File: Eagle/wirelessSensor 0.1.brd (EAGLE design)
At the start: 25.1 x 25.4 mm, 22 parts, among them U1 HDC1080, U2 PIC16F1823-X_SL, X1 22-23-2021

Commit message: Started working on the ESP8266, having some trouble with buffer overrun on the PIC.  Started some board layout
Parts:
- added R4: 10k, rcl:R0603
- moved U$1 45.5 mm to (5.08, 34.3)
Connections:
- new net N$7: R4.1, U$1.3
- net N$1: now also U$1.22; no longer U$1.21
- net N$8: now also U$1.21; no longer U$1.22
- net VCC: now also R4.2
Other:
- board size 25.1 x 25.4 mm -> 25.1 x 50.8 mm
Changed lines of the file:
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@@
 <?xml version="1.0" encoding="utf-8"?>
 <!DOCTYPE eagle SYSTEM "eagle.dtd">
-<eagle version="7.7.0">
+<eagle version="7.6.0">
 <drawing>
 <settings>
@@
 <plain>
 <wire x1="0" y1="0" x2="25.07" y2="0" width="0" layer="20"/>
-<wire x1="25.07" y1="0" x2="25.07" y2="25.39" width="0" layer="20"/>
-<wire x1="25.07" y1="25.39" x2="0" y2="25.39" width="0" layer="20"/>
-<wire x1="0" y1="25.39" x2="0" y2="0" width="0" layer="20"/>
+<wire x1="25.07" y1="0" x2="25.07" y2="50.79" width="0" layer="20"/>
+<wire x1="25.07" y1="50.79" x2="0" y2="50.79" width="0" layer="20"/>
+<wire x1="0" y1="50.79" x2="0" y2="0" width="0" layer="20"/>
 </plain>
 <attributes>
@@
 <element name="LED1" library="led" package="CHIP-LED0603" value="" x="22.86" y="10.16"/>
 <element name="R3" library="rcl" package="R0603" value="330" x="20.32" y="10.16" rot="R90"/>
-<element name="U$1" library="wirelessSensor" package="ESP8266-12E" value="ESP8266-12E" x="-21.59" y="-2.54"/>
+<element name="U$1" library="wirelessSensor" package="ESP8266-12E" value="ESP8266-12E" x="5.08" y="34.29"/>
+<element name="R4" library="rcl" package="R0603" value="10k" x="1.27" y="40.64" rot="R270"/>
 </elements>
 <signals>
@@
 <contactref element="C4" pad="1"/>
 <contactref element="C3" pad="1"/>
+<contactref element="R4" pad="2"/>
 <wire x1="19.47" y1="16.51" x2="22.86" y2="21.59" width="0" layer="19" extent="1-1"/>
 <wire x1="10.3378" y1="15.24" x2="19.47" y2="16.51" width="0" layer="19" extent="1-1"/>
@@
 <wire x1="4.205" y1="1.27" x2="4.205" y2="3.81" width="0" layer="19" extent="1-1"/>
 <wire x1="3.81" y1="24.13" x2="5.209996875" y2="17.78" width="0" layer="19" extent="1-1"/>
-<wire x1="-21.59" y1="-1.04" x2="4.205" y2="1.27" width="0" layer="19" extent="1-1"/>
+<wire x1="1.27" y1="39.79" x2="4.205" y2="1.27" width="0" layer="19" extent="1-1"/>
+<wire x1="5.08" y1="35.79" x2="1.27" y2="39.79" width="0" layer="19" extent="1-1"/>
 </signal>
 <signal name="GND">
@@
 <wire x1="5.955" y1="3.81" x2="5.955" y2="6.35" width="0" layer="19" extent="1-1"/>
 <wire x1="5.955" y1="1.27" x2="5.955" y2="3.81" width="0" layer="19" extent="1-1"/>
-<wire x1="-5.59" y1="-1.04" x2="5.955" y2="1.27" width="0" layer="19" extent="1-1"/>
+<wire x1="21.08" y1="35.79" x2="5.955" y2="1.27" width="0" layer="19" extent="1-1"/>
 </signal>
 <signal name="N$2">
@@
 </signal>
 <signal name="N$8">
-<contactref element="U$1" pad="22"/>
 <contactref element="U2" pad="6"/>
 <contactref element="TX" pad="TP"/>
+<contactref element="U$1" pad="21"/>
 <wire x1="1.27" y1="3.81" x2="10.3378" y2="8.89" width="0" layer="19" extent="1-1"/>
-<wire x1="-5.59" y1="12.96" x2="1.27" y2="3.81" width="0" layer="19" extent="1-1"/>
+<wire x1="21.08" y1="47.79" x2="1.27" y2="3.81" width="0" layer="19" extent="1-1"/>
 </signal>
 <signal name="N$1">
 <contactref element="U2" pad="5"/>
 <contactref element="RX" pad="TP"/>
-<contactref element="U$1" pad="21"/>
+<contactref element="U$1" pad="22"/>
 <wire x1="1.27" y1="1.27" x2="10.3378" y2="10.16" width="0" layer="19" extent="1-1"/>
-<wire x1="-5.59" y1="10.96" x2="1.27" y2="1.27" width="0" layer="19" extent="1-1"/>
+<wire x1="21.08" y1="49.79" x2="1.27" y2="1.27" width="0" layer="19" extent="1-1"/>
+</signal>
+<signal name="N$7">
+<contactref element="R4" pad="1"/>
+<contactref element="U$1" pad="3"/>
+<wire x1="5.08" y1="45.79" x2="1.27" y2="41.49" width="0" layer="19" extent="1-1"/>
 </signal>
 </signals>

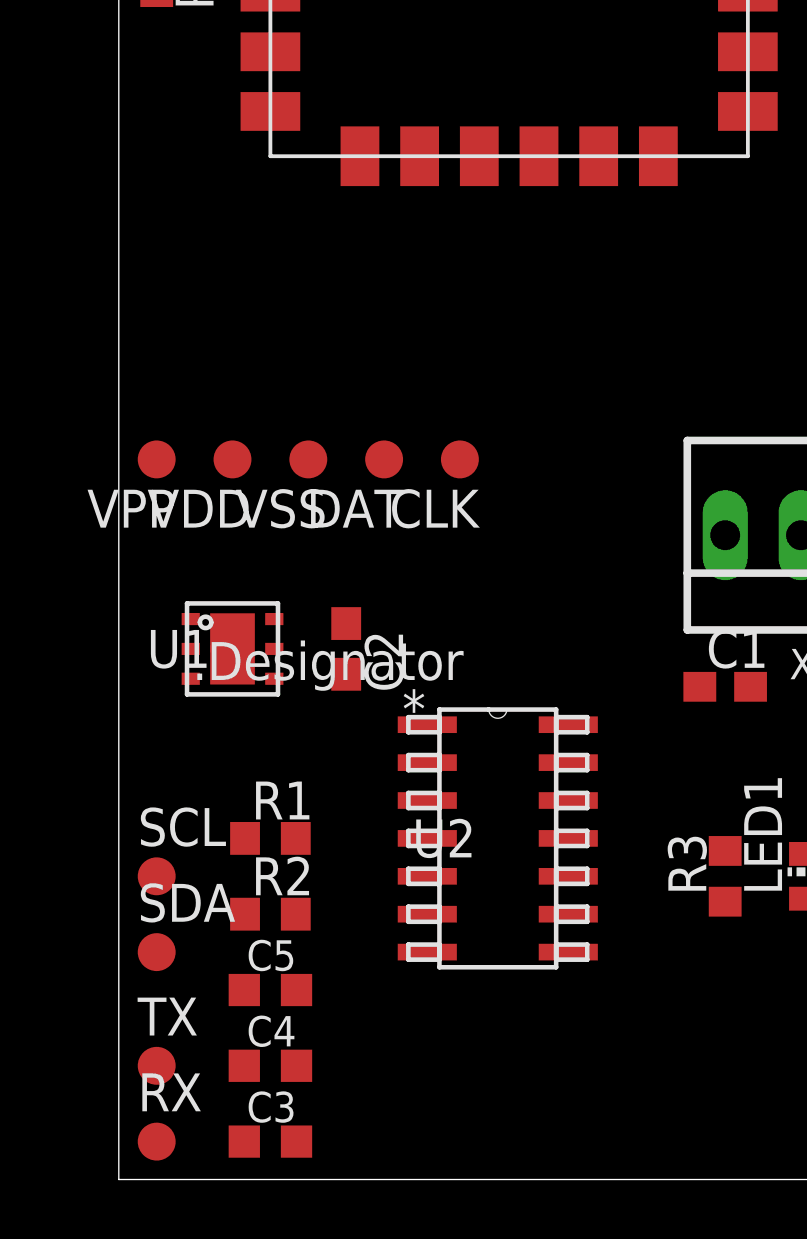
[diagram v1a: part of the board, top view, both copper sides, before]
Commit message: Wrapping up the schematic before board order; minor firmware adjustments; added CAM file for Gerber generation
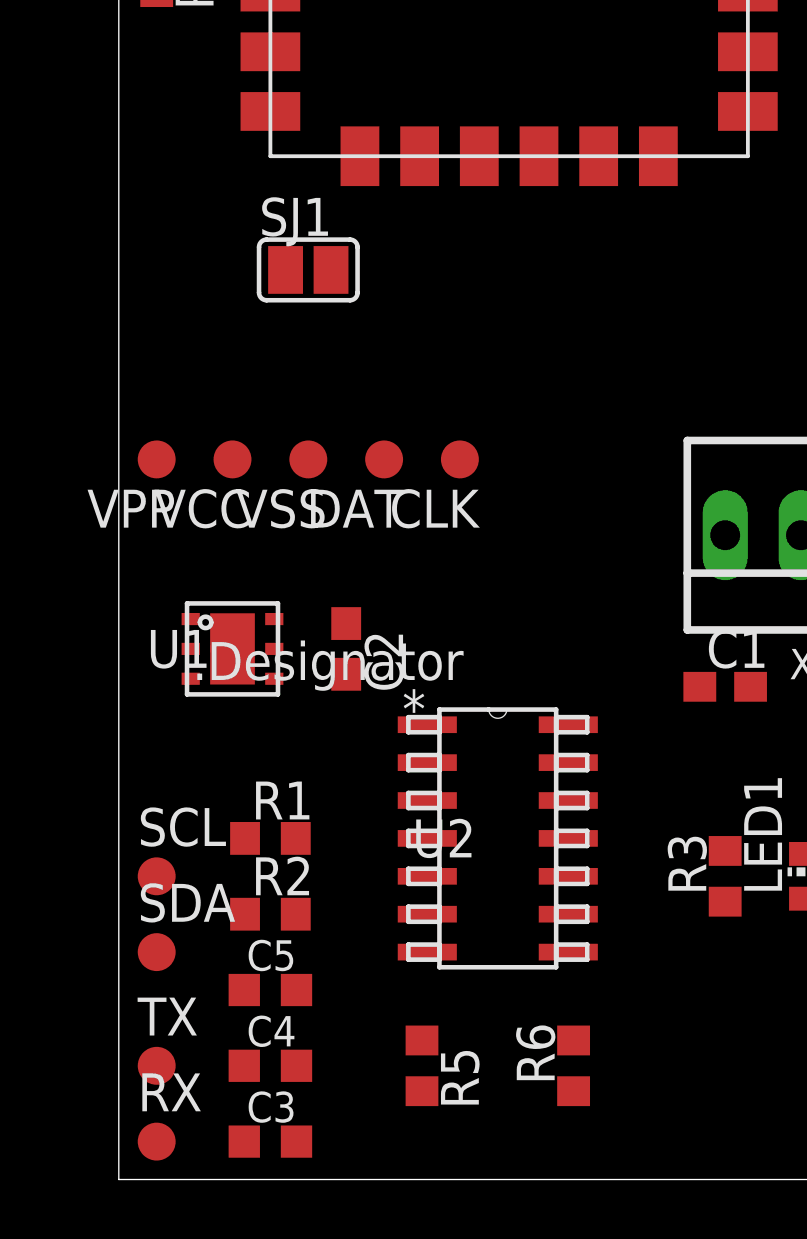
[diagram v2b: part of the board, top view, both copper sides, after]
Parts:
- added R5, R6: SEL, rcl:R0603
- added SJ1: (no value), jumper:SJ
- renumbered VDD to VCC
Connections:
- new net N$12: SJ1.1, U$1.2
- new net N$9: R5.1, R6.2, SJ1.2, U2.3
- net GND: now also R6.1
- net VCC: now also R5.2
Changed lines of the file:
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@@
 <?xml version="1.0" encoding="utf-8"?>
 <!DOCTYPE eagle SYSTEM "eagle.dtd">
-<eagle version="7.6.0">
+<eagle version="7.7.0">
 <drawing>
 <settings>
@@
 </element>
 <element name="U2" library="wirelessSensor" package="SOIC14-N_MC" value="PIC16F1823-X_SL" x="12.7" y="11.43"/>
-<element name="VDD" library="testpad" package="B1,27" value="TPB1,27" x="3.81" y="24.13" rot="R180">
+<element name="VCC" library="testpad" package="B1,27" value="TPB1,27" x="3.81" y="24.13" rot="R180">
 <attribute name="TP_SIGNAL_NAME" value="" x="3.81" y="24.13" size="1.778" layer="27" rot="R180" display="off"/>
 </element>
@@
 <element name="U$1" library="wirelessSensor" package="ESP8266-12E" value="ESP8266-12E" x="5.08" y="34.29"/>
 <element name="R4" library="rcl" package="R0603" value="10k" x="1.27" y="40.64" rot="R270"/>
+<element name="R5" library="rcl" package="R0603" value="SEL" x="10.16" y="3.81" rot="R270"/>
+<element name="R6" library="rcl" package="R0603" value="SEL" x="15.24" y="3.81" rot="R90"/>
+<element name="SJ1" library="jumper" package="SJ" value="" x="6.35" y="30.48"/>
 </elements>
 <signals>
@@
 <contactref element="U2" pad="1"/>
 <contactref element="U1" pad="5"/>
-<contactref element="VDD" pad="TP"/>
+<contactref element="VCC" pad="TP"/>
 <contactref element="C2" pad="1"/>
 <contactref element="C5" pad="1"/>
@@
 <contactref element="C3" pad="1"/>
 <contactref element="R4" pad="2"/>
+<contactref element="R5" pad="2"/>
 <wire x1="19.47" y1="16.51" x2="22.86" y2="21.59" width="0" layer="19" extent="1-1"/>
 <wire x1="10.3378" y1="15.24" x2="19.47" y2="16.51" width="0" layer="19" extent="1-1"/>
@@
 <wire x1="4.205" y1="3.81" x2="4.205" y2="6.35" width="0" layer="19" extent="1-1"/>
 <wire x1="4.205" y1="1.27" x2="4.205" y2="3.81" width="0" layer="19" extent="1-1"/>
+<wire x1="10.16" y1="2.96" x2="4.205" y2="1.27" width="0" layer="19" extent="1-1"/>
 <wire x1="3.81" y1="24.13" x2="5.209996875" y2="17.78" width="0" layer="19" extent="1-1"/>
-<wire x1="1.27" y1="39.79" x2="4.205" y2="1.27" width="0" layer="19" extent="1-1"/>
-<wire x1="5.08" y1="35.79" x2="1.27" y2="39.79" width="0" layer="19" extent="1-1"/>
+<wire x1="5.08" y1="35.79" x2="3.81" y2="24.13" width="0" layer="19" extent="1-1"/>
+<wire x1="1.27" y1="39.79" x2="5.08" y2="35.79" width="0" layer="19" extent="1-1"/>
 </signal>
 <signal name="GND">
@@
 <contactref element="C4" pad="2"/>
 <contactref element="C3" pad="2"/>
+<contactref element="R6" pad="1"/>
+<wire x1="20.32" y1="21.59" x2="21.08" y2="35.79" width="0" layer="19" extent="1-1"/>
 <wire x1="21.17" y1="16.51" x2="20.32" y2="21.59" width="0" layer="19" extent="1-1"/>
 <wire x1="15.0622" y1="15.24" x2="21.17" y2="16.51" width="0" layer="19" extent="1-1"/>
@@
 <wire x1="5.955" y1="3.81" x2="5.955" y2="6.35" width="0" layer="19" extent="1-1"/>
 <wire x1="5.955" y1="1.27" x2="5.955" y2="3.81" width="0" layer="19" extent="1-1"/>
-<wire x1="21.08" y1="35.79" x2="5.955" y2="1.27" width="0" layer="19" extent="1-1"/>
+<wire x1="15.24" y1="2.96" x2="5.955" y2="1.27" width="0" layer="19" extent="1-1"/>
 </signal>
 <signal name="N$2">
@@
 <wire x1="5.08" y1="45.79" x2="1.27" y2="41.49" width="0" layer="19" extent="1-1"/>
 </signal>
+<signal name="N$9">
+<contactref element="R6" pad="2"/>
+<contactref element="R5" pad="1"/>
+<contactref element="U2" pad="3"/>
+<contactref element="SJ1" pad="2"/>
+<wire x1="10.16" y1="4.66" x2="10.3378" y2="12.7" width="0" layer="19" extent="1-1"/>
+<wire x1="15.24" y1="4.66" x2="10.16" y2="4.66" width="0" layer="19" extent="1-1"/>
+<wire x1="7.112" y1="30.48" x2="10.16" y2="4.66" width="0" layer="19" extent="1-1"/>
+</signal>
+<signal name="N$12">
+<contactref element="SJ1" pad="1"/>
+<contactref element="U$1" pad="2"/>
+<wire x1="5.588" y1="30.48" x2="5.08" y2="47.79" width="0" layer="19" extent="1-1"/>
+</signal>
 </signals>

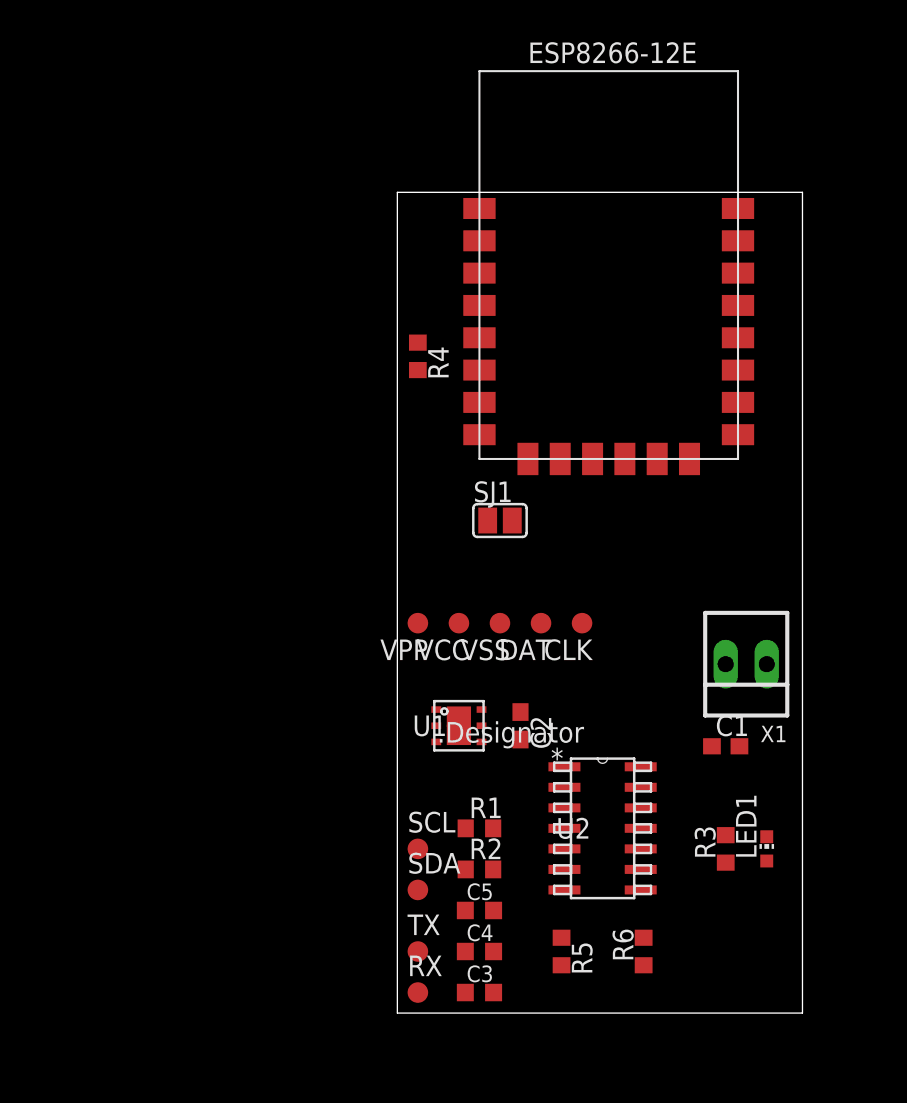
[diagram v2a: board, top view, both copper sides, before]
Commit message: More work on the PCB, added some SeeedStudio specific files (cam generator, DRC rules)
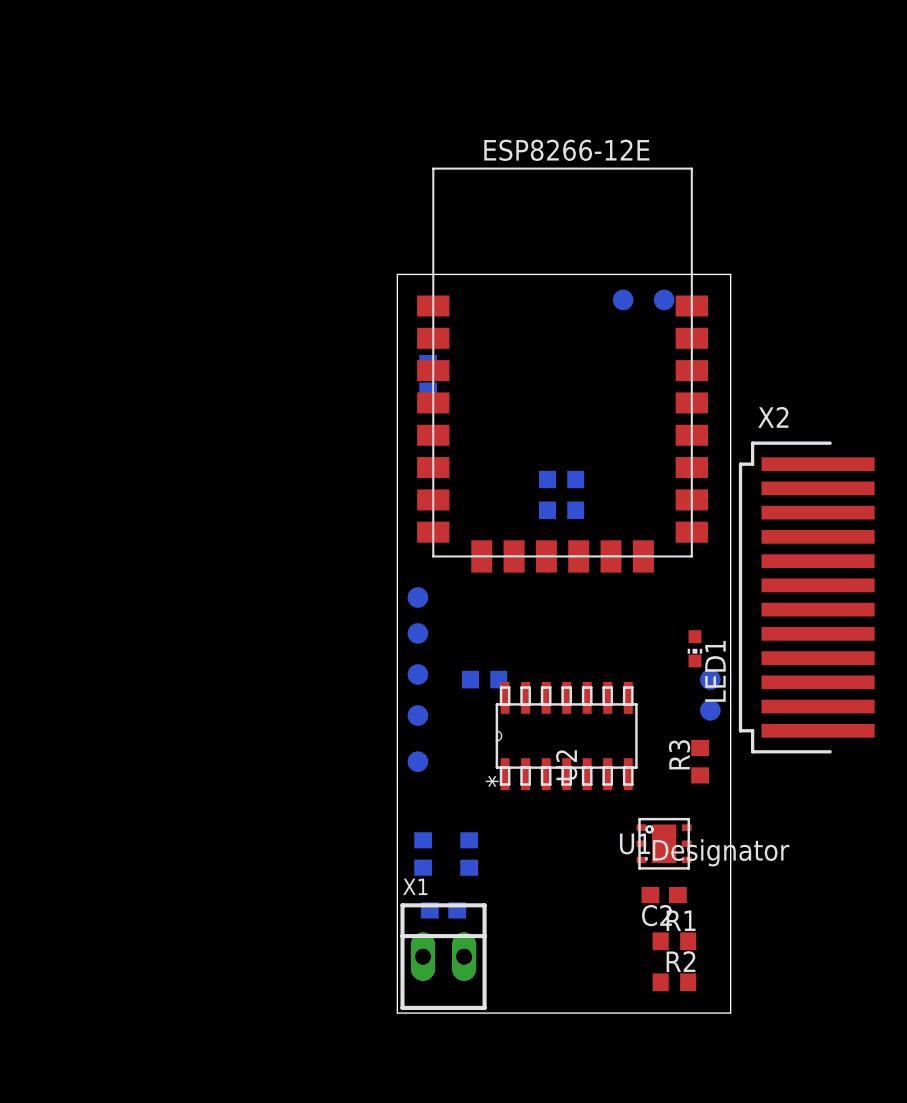
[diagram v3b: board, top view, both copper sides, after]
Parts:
- removed SJ1: (no value), jumper:SJ
- added X2: 87438-12, con-molex:87438-12
- moved RX 45.5 mm to (16.5, 44.1), flipped to the bottom
- moved TX 42.3 mm to (14.0, 44.1), flipped to the bottom
- moved C3 30.3 mm to (10.2, 31.1), flipped to the bottom, turned to 180 degrees
- moved C4 29.6 mm to (10.2, 33.0), flipped to the bottom, turned to 180 degrees
- moved X1 26.0 mm to (2.86, 3.49), turned to 0 degrees
- moved SDA 22.3 mm to (19.4, 20.6), flipped to the bottom
- moved C1 20.2 mm to (2.86, 6.35), flipped to the bottom, turned to 180 degrees
- moved SCL 20.0 mm to (19.4, 18.7), flipped to the bottom
- moved U1 14.6 mm to (16.5, 10.5)
- moved C5 14.3 mm to (5.40, 20.6), flipped to the bottom, turned to 180 degrees
- moved R1 13.9 mm to (17.1, 4.45)
- moved R2 13.9 mm to (17.1, 1.91)
- moved C2 13.7 mm to (16.5, 7.30), turned to 180 degrees
- moved LED1 13.2 mm to (18.4, 22.5), turned to 180 degrees
- moved R6 12.4 mm to (4.45, 9.84), flipped to the bottom
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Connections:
- removed net N$12: SJ1.1, U$1.2
- net N$9: no longer SJ1.2
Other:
- board size 25.1 x 50.8 mm -> 20.6 x 45.7 mm
